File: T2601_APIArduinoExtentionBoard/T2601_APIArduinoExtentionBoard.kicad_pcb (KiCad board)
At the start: 2 copper layers, 59.8 x 90 mm, 95 parts, among them J1 Conn_01x10_Socket, J11 Conn_01x04_Pin, J12 Screw_Terminal_01x02, J13 Conn_01x04_Pin, J14 Screw_Terminal_01x02, J15 Conn_02x08_Counter_Clockwise, J2 Conn_01x10_Socket, J3 Conn_01x10_Socket, J4 Conn_01x10_Socket, J5 Screw_Terminal_01x08, J6 Screw_Terminal_01x08, J7 Conn_02x03_Counter_Clockwise, J8 Conn_01x04, J9 Conn_02x08_Counter_Clockwise, U1 ATMEGA328P-AU, X1 X322516MOB4SI

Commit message: Kicad Modification, switch ATMEGA328P to ATMEGA328PB, schematic modification + rerouting, V0 version, no verification
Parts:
- removed C4: 100nF, PCM_JLCPCB:C_0402
- removed D13: Red, PCM_JLCPCB:D_0805
- removed R2: 1kΩ, PCM_JLCPCB:R_0402
- removed U1: ATMEGA328P-AU, T2601_APIArduinoExtentionBoard_Lib:TQFP-32_L7.0-W7.0-P0.80-LS9.0-BL
- added C9: 100nF, PCM_JLCPCB:C_0402, F.Cu at (160.8, 61.7)
- added D27: Red, PCM_JLCPCB:D_0805, F.Cu at (154.9, 48.5)
- added D28: Green, PCM_JLCPCB:D_0805, F.Cu at (148.1, 48.5)
- added D29: Yellow, PCM_JLCPCB:D_0805, F.Cu at (145.9, 61.4)
- added R26: 1kΩ, PCM_JLCPCB:R_0402, F.Cu at (152.4, 48.5)
- added R27: 1kΩ, PCM_JLCPCB:R_0402, F.Cu at (150.4, 48.5)
- added R28: 1kΩ, PCM_JLCPCB:R_0402, F.Cu at (144.3, 63.0)
- added U2: ATmega328PB-A, Package_QFP:TQFP-32_7x7mm_P0.8mm, F.Cu at (156.0, 57.0)
- moved C7 1.66 mm to (150.9, 51.8), turned to -135 degrees
- moved D8 1.58 mm to (138.8, 58.4)
- moved D7 1.58 mm to (138.8, 60.6)
- moved C3 0.72 mm to (151.6, 52.6), turned to -135 degrees
- moved C8 0.46 mm to (158.6, 62.9)
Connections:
- J4 pad 1: P14 -> P32
- J4 pad 2: P13 -> P14
- J4 pad 3: P12 -> P13
- J4 pad 4: P11 -> P12
- J4 pad 7: P10 -> P11
- J4 pad 8: P9 -> P10
- J4 pad 9: P2 -> P9
- J8 pad 2: P32 -> P2
- R10 pad 1: P10 -> P11
- R11 pad 1: P11 -> P12
- R12 pad 1: P12 -> P13
- R13 pad 1: P13 -> P14
- R14 pad 1: P14 -> P32
- R8 pad 1: P2 -> P9
- R9 pad 1: P9 -> P10
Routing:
- net P2: track 46.4 -> 28.5 mm, vias 0 -> 1
- net P32: track 27.2 -> 42.5 mm, vias 1 -> 2
- net P6: track 0.00 -> 9.81 mm, vias 0 -> 2
- net P3: track 0.00 -> 8.71 mm
- net RESET: track 45.5 -> 41.8 mm
- net SCK: track 4.03 -> 0.35 mm
- net P11: track 26.9 -> 30.3 mm
- net +5V: track 64.6 -> 68.0 mm
- net GND: track 59.2 -> 62.0 mm, vias 26 -> 27
- net Net-(U2-AREF): track 0.00 -> 2.58 mm
- net P10: track 29.6 -> 31.9 mm
- net P25: track 34.4 -> 36.6 mm
- net TX: track 32.0 -> 29.9 mm, vias 2 -> 4
- net Net-(U1-AREF): track 1.76 -> 0.00 mm
- net Net-(D27-Pad1): track 0.00 -> 1.74 mm
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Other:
- board text added: "~P1"
- board text added: "~P10"
- board text added: "~P13"
- board text added: "~P14"
- board text added: "~P32"
- board text added: "~P9"
- board text removed: "P1"
- board text removed: "P10"
- board text removed: "P13"
- board text removed: "P14"
- board text removed: "P2"
- board text removed: "P9"

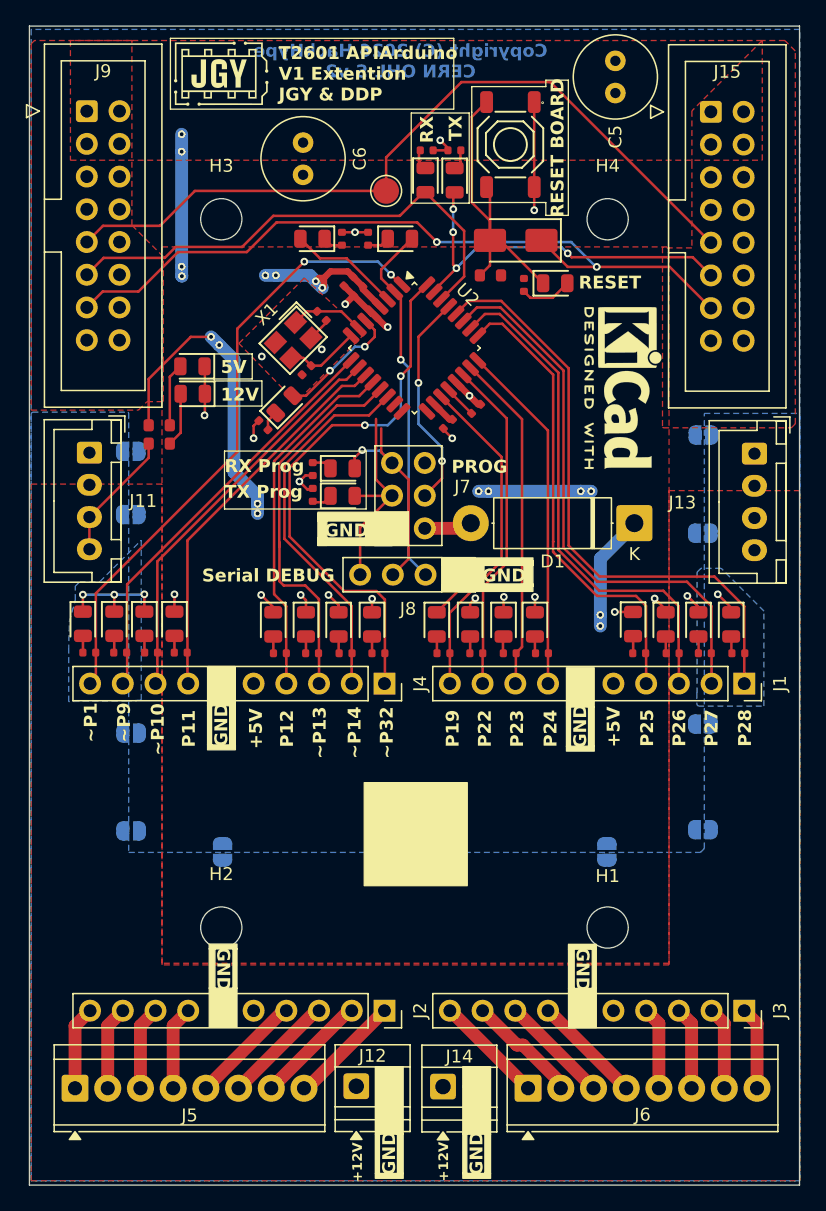
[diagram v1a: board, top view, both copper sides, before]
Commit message: Switch to 4 layers PCB
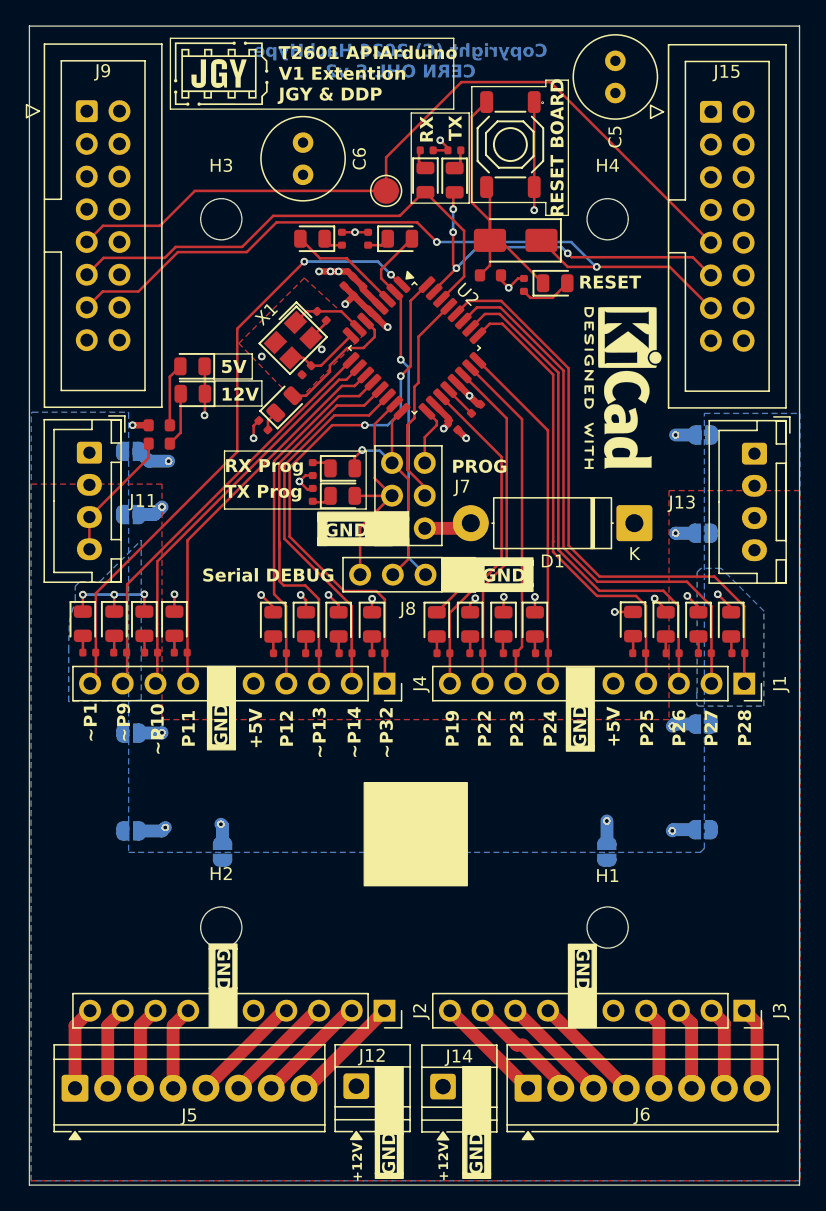
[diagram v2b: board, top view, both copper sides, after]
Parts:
- moved C8 0.42 mm to (159.0, 63.0), turned to -45 degrees
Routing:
- net +5V: track 68.0 -> 12.6 mm, vias 18 -> 6
- net GND: track 62.0 -> 85.1 mm, vias 27 -> 39
- net SCK: track 0.35 -> 5.06 mm
- net MOSI: track 16.5 -> 18.4 mm
- net MISO: track 17.2 -> 18.4 mm
- net RESET: track 41.8 -> 41.4 mm, vias 2 -> 0
- net P6: track 9.81 -> 10.1 mm, vias 2 -> 0
- added copper zone on In1.Cu, net +5V
- added copper zone on In2.Cu, net GND
- removed copper zone on F.Cu, net +5V
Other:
- copper layers 2 -> 4

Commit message: Modification Board to 4 layers, finition routing et re organisation des composants (leds statuts condo alim + reset
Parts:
- added RX: TestPoint, TestPoint:TestPoint_Loop_D2.50mm_Drill1.0mm_LowProfile, F.Cu at (147.6, 43.6)
- U.B.: renamed from TP1; footprint TestPoint:TestPoint_Pad_D2.0mm -> TestPoint:TestPoint_Loop_D2.50mm_Drill1.0mm_LowProfile
- moved G*** 68.1 mm to (149.0, 103.3)
- moved R26 12.8 mm to (140.0, 51.3), turned to 135 degrees
- moved D26 12.6 mm to (155.7, 46.2), turned to -90 degrees
- moved R27 11.7 mm to (139.2, 52.1), turned to 135 degrees
- moved R28 11.7 mm to (138.4, 52.8)
- moved D27 10.4 mm to (144.8, 51.1), turned to -45 degrees
- moved C6 9.28 mm to (140.7, 34.6)
- moved U.B. 8.60 mm to (147.6, 38.9)
- moved D29 8.29 mm to (141.5, 54.4), turned to -45 degrees
- moved R25 8.11 mm to (157.7, 47.6), turned to 180 degrees
- moved R5 6.97 mm to (157.8, 45.8), turned to 90 degrees
- moved D28 6.44 mm to (143.2, 52.7), turned to -45 degrees
- moved D11 6.11 mm to (150.9, 42.6)
- moved D12 6.11 mm to (153.2, 42.6)
- moved R3 6.11 mm to (151.0, 40.3)
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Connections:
- D11 pad 2: RX -> TX
- D12 pad 2: TX -> RX
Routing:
- net P6: track 10.1 -> 18.5 mm
- net TX: track 29.9 -> 36.6 mm, vias 4 -> 1
- net P2: track 28.5 -> 34.0 mm
- net GND: track 85.1 -> 80.2 mm, vias 39 -> 45
- net RESET: track 41.4 -> 46.4 mm
- net GEN_RESET: track 59.1 -> 54.9 mm, vias 2 -> 1
- net P3: track 8.71 -> 12.5 mm
- net Net-(D27-Pad1): track 1.74 -> 4.33 mm
- net Net-(D26-Pad2): track 4.04 -> 1.72 mm
- net Net-(D28-Pad1): track 1.56 -> 3.13 mm
- net RX: track 39.5 -> 41.0 mm
- net UART_BACK: track 60.7 -> 59.1 mm
- net P1: track 48.0 -> 48.8 mm
- net Net-(D29-Pad1): track 1.56 -> 2.24 mm
- net +5V: track 12.6 -> 12.0 mm
- removed copper zone on B.Cu, net GND
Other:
- board text added: "STATUS"

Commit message: Resolution de diversse ISSUE, position UART, Rerouting, modif VIA
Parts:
- moved J15 48.5 mm to (130.6, 38.6)
- moved J9 48.4 mm to (178.9, 38.7)
- moved C9 0.90 mm to (160.1, 61.1)
- renumbered U.B. to TP1, RX to TP2
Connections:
- TP2 pad 1: RX -> TX
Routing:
- net RX: track 41.0 -> 52.2 mm
- net TX: track 36.6 -> 39.5 mm, vias 1 -> 0
- net P32: track 42.5 -> 40.8 mm
- net P1: track 48.8 -> 50.2 mm, vias 2 -> 0
- net Net-(U2-AREF): track 2.58 -> 1.68 mm
- net GND: track 80.2 -> 79.5 mm
- net P6: track 18.5 -> 19.1 mm
